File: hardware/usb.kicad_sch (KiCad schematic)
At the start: 30 parts, among them J2 USB_C_Receptacle_USB2.0_14P, J3 USB_C_Receptacle_USB2.0_14P, J4 USB_A_Stacked, J5 USB_C_Receptacle_USB2.0_14P, U10 TPD2EUSB30, U11 SY6280AAC, U12 HUSB237, U4 SY6280AAC, U5 SY6280AAC, U6 TPD2EUSB30, U7 TPD2EUSB30, U8 SY6280AAC, U9 TPD2EUSB30

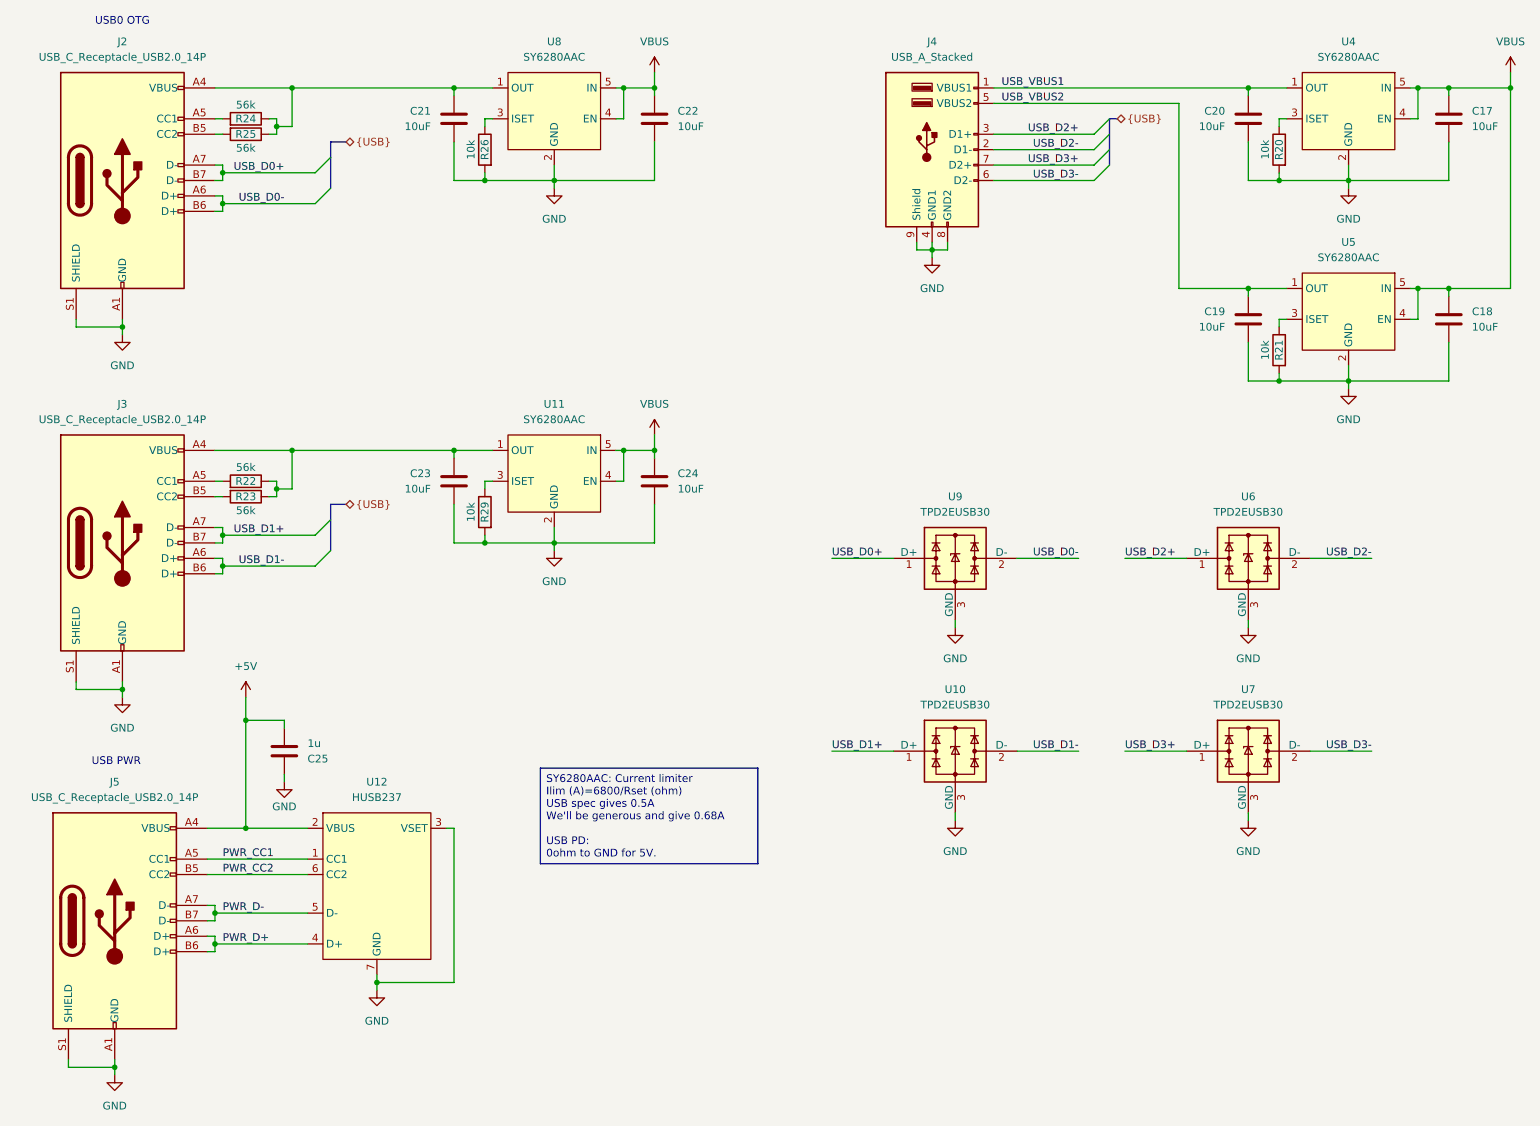
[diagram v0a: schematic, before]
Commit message: Decoupled DDR3 and drew RJ45 connector
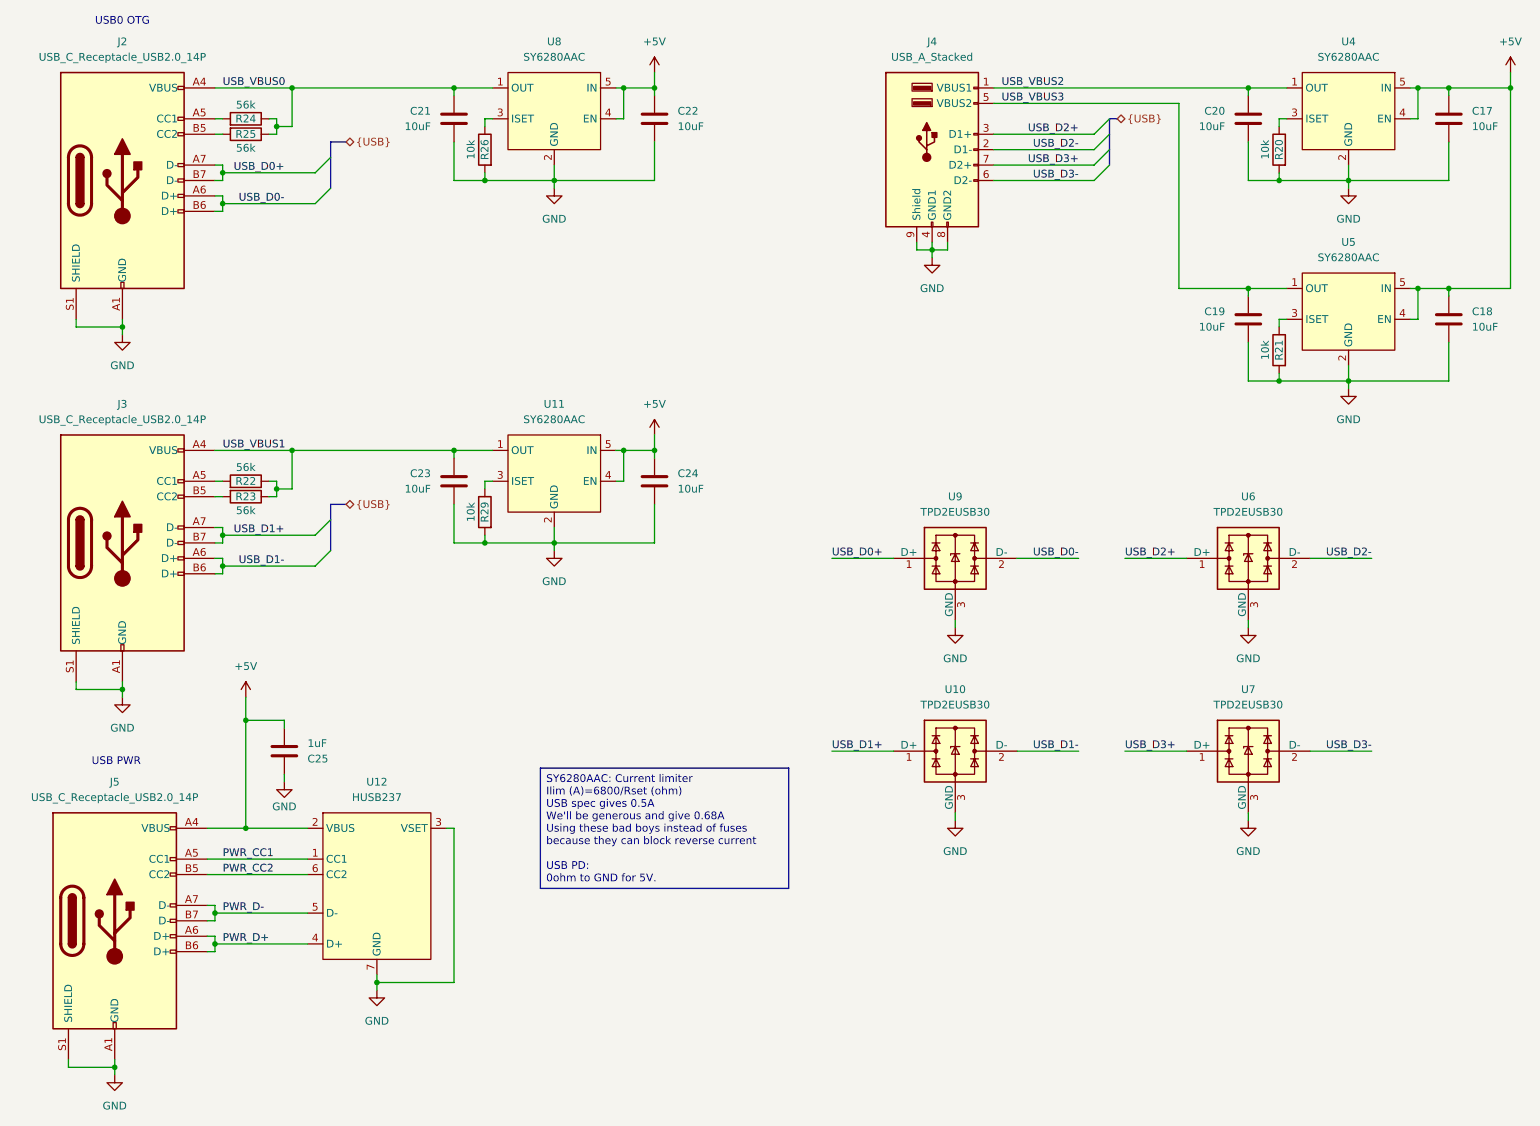
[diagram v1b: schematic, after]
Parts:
- C17, C18, C19, C20, C21, C22, C23, C24: LCSC Part # C15525 -> C19702
- C25: value 1u -> 1uF; LCSC Part # (none) -> C52923
- R20, R21, R26, R29: LCSC Part # (none) -> C25744
- R22, R23, R24, R25: LCSC Part # (none) -> C25796
- U11, U4, U5, U8: LCSC Part # (none) -> C55136
- U12: LCSC Part # (none) -> C22373734
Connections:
- net VBUS is gone; now on net +5V: C17.1, C18.1, C22.1, C24.1, U11.4 (EN), U11.5 (IN), U4.4 (EN), U4.5 (IN), U5.4 (EN), U5.5 (IN), U8.4 (EN), U8.5 (IN)
- net USB_VBUS1: now also C23.1, J3.A4 (VBUS), J3.A9 (VBUS), J3.B4 (VBUS), J3.B9 (VBUS), R22.1, R23.1, U11.1 (OUT); no longer C20.1, J4.1 (VBUS1), U4.1 (OUT)
- net USB_VBUS2: now also C20.1, J4.1 (VBUS1), U4.1 (OUT); no longer C19.1, J4.5 (VBUS2), U5.1 (OUT)
- net USB_VBUS0: now reaches C21.1, J2.A4 (VBUS), J2.A9 (VBUS), J2.B4 (VBUS), J2.B9 (VBUS), R24.1, R25.1, U8.1 (OUT)
- new net USB_VBUS3: C19.1, J4.5 (VBUS2), U5.1 (OUT)
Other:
- company: (none) -> Icy Electronics
- title: (none) -> Icepi CM0

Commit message: Initial layout
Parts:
- added U16: TPD2EUSB30, Package_TO_SOT_SMD:Texas_DRT-3, symbol Power_Protection:TPD2EUSB30
- J3: renamed from J5; footprint Connector_USB:USB_C_Receptacle_HRO_TYPE-C-31-M-12 -> cm0:USB_C_Receptacle_HRO_TYPE-C-31-M-12
- J4: renamed from J2; footprint Connector_USB:USB_C_Receptacle_HRO_TYPE-C-31-M-12 -> cm0:USB_C_Receptacle_HRO_TYPE-C-31-M-12
- J5: renamed from J3; footprint Connector_USB:USB_C_Receptacle_HRO_TYPE-C-31-M-12 -> cm0:USB_C_Receptacle_HRO_TYPE-C-31-M-12
- renumbered C25 to C36, C21 to C37, C23 to C38, C22 to C39, C24 to C40, C20 to C41, C19 to C42, C17 to C43, C18 to C44, J4 to J6, R24 to R23, R25 to R24, R22 to R25, R23 to R26, R26 to R27, R29 to R28, R20 to R29, R21 to R30, U6 to U11, U7 to U12, U4 to U13, U5 to U14, U12 to U6, U8 to U7, U11 to U8
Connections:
- net GND: now also U16.3 (GND)
- net PWR_D+: now also U16.1 (D+)
- net PWR_D-: now also U16.2 (D-)
